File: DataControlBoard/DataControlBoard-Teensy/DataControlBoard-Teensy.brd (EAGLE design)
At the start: 66 x 88.9 mm, 40 parts, among them IC1 74LS165D, IC2 74LS165D, IC3 74AHC1G04DCK, J1 RS-Interface, J2 Pwr-Conn, J3 Static RPi, J4 Magnet RPi, J5 Boom Cam RPi, U1 MAX3232, U2 3V3REG

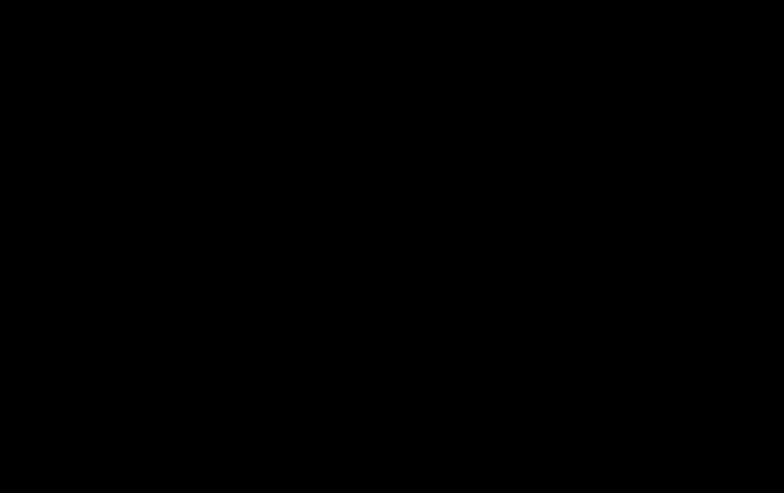
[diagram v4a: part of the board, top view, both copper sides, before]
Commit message: Minor schematic changes, added GND merges and header for LIDAR
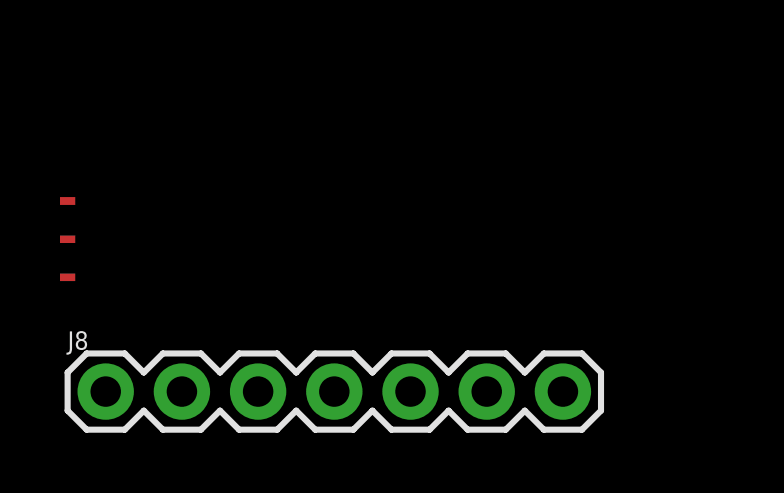
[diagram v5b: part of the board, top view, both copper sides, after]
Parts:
- added J8: (no value), SparkFun-Connectors:1X07
- added U$1, U$2, U$3: GND-MERGER, RPi-Parts:GND-MERGER
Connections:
- new net DTR: J8.2
- new net GND-ANALOG: J1.P21, U$1.P$2
- new net PDB-GND: J1.P7, U$3.P$2
- new net RX: J8.5
- new net TX: J8.6
- new net VS: J8.4
- new net VS_2: J8.1
- net GND: now also J8.3, J8.7, U$1.P$1, U$2.P$1, U$3.P$1; no longer J1.P18, J1.P19, J1.P21, J1.P7
- net PDB-STROBE-3V3: now also B1.22; no longer B1.2
- net RS232-GND: now also U$2.P$2
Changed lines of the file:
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@@
 <attribute name="VALUE" x="-71.12" y="-11.303" size="0.6096" layer="27" font="vector" ratio="20" align="top-center"/>
+</element>
+<element name="U$1" library="RPi-Parts" package="GND-MERGER" value="GND-MERGER" x="-85.09" y="-48.26" smashed="yes"/>
+<element name="U$2" library="RPi-Parts" package="GND-MERGER" value="GND-MERGER" x="-85.09" y="-49.53" smashed="yes"/>
+<element name="U$3" library="RPi-Parts" package="GND-MERGER" value="GND-MERGER" x="-85.09" y="-50.8" smashed="yes"/>
+<element name="J8" library="SparkFun-Connectors" library_urn="urn:adsk.eagle:library:513" package="1X07" package3d_urn="urn:adsk.eagle:package:38129/1" value="" x="-83.82" y="-54.61" smashed="yes">
+<attribute name="NAME" x="-85.09" y="-53.213" size="0.6096" layer="25" font="vector" ratio="20"/>
+<attribute name="VALUE" x="-85.09" y="-56.642" size="0.6096" layer="27" font="vector" ratio="20"/>
 </element>
 </elements>
 <signals>
 <signal name="GND">
-<contactref element="J1" pad="P24"/>
-<contactref element="J1" pad="P25"/>
-<contactref element="J1" pad="P7"/>
-<contactref element="J1" pad="P21"/>
-<contactref element="J1" pad="P19"/>
-<contactref element="J1" pad="P18"/>
 <contactref element="J1" pad="SHLD1"/>
 <contactref element="J1" pad="SHLD2"/>
@@
 <contactref element="C5" pad="2"/>
 <contactref element="IC3" pad="3"/>
+<contactref element="J1" pad="P25"/>
+<contactref element="J1" pad="P24"/>
+<contactref element="U$1" pad="P$1"/>
+<contactref element="U$2" pad="P$1"/>
+<contactref element="U$3" pad="P$1"/>
+<contactref element="J8" pad="7"/>
+<contactref element="J8" pad="3"/>
 <wire x1="87.63" y1="68.26" x2="92.71" y2="68.26" width="0" layer="19" extent="1-1"/>
 <wire x1="58.42" y1="85.09" x2="87.63" y2="68.26" width="0" layer="19" extent="1-1"/>
@@
 <wire x1="17.2466" y1="70.485" x2="23.3934" y2="78.105" width="0" layer="19" extent="1-1"/>
 <wire x1="17.145" y1="57.6834" x2="17.2466" y2="70.485" width="0" layer="19" extent="1-1"/>
-<wire x1="7.62" y1="55.88" x2="17.145" y2="57.6834" width="0" layer="19" extent="1-1"/>
-<wire x1="5.08" y1="55.245" x2="7.62" y2="55.88" width="0" layer="19" extent="1-1"/>
-<wire x1="5.08" y1="53.975" x2="5.08" y2="55.245" width="0" layer="19" extent="1-1"/>
-<wire x1="5.08" y1="57.785" x2="5.08" y2="55.245" width="0" layer="19" extent="1-1"/>
-<wire x1="5.08" y1="61.595" x2="5.08" y2="57.785" width="0" layer="19" extent="1-1"/>
+<wire x1="24.765" y1="51.5366" x2="17.145" y2="57.6834" width="0" layer="19" extent="1-1"/>
+<wire x1="5.08" y1="61.595" x2="17.145" y2="57.6834" width="0" layer="19" extent="1-1"/>
 <wire x1="5.08" y1="62.865" x2="5.08" y2="61.595" width="0" layer="19" extent="1-1"/>
 <wire x1="3.81" y1="68.1355" x2="5.08" y2="62.865" width="0" layer="19" extent="1-1"/>
-<wire x1="24.765" y1="51.5366" x2="17.145" y2="57.6834" width="0" layer="19" extent="1-1"/>
-<wire x1="3.81" y1="43.6245" x2="5.08" y2="53.975" width="0" layer="19" extent="1-1"/>
+<wire x1="3.81" y1="43.6245" x2="5.08" y2="61.595" width="0" layer="19" extent="1-1"/>
 <wire x1="3.81" y1="27.4955" x2="3.81" y2="43.6245" width="0" layer="19" extent="1-1"/>
 <wire x1="5.08" y1="15.875" x2="3.81" y2="27.4955" width="0" layer="19" extent="1-1"/>
@@
 <wire x1="-63.5" y1="47.31" x2="-63.5" y2="45.4" width="0" layer="19" extent="1-1"/>
 <wire x1="-73.01" y1="-4.66" x2="-63.5" y2="45.4" width="0" layer="19" extent="1-1"/>
+<wire x1="-85.217" y1="-48.26" x2="-73.01" y2="-4.66" width="0" layer="19" extent="1-1"/>
+<wire x1="-85.217" y1="-49.53" x2="-85.217" y2="-48.26" width="0" layer="19" extent="1-1"/>
+<wire x1="-85.217" y1="-50.8" x2="-85.217" y2="-49.53" width="0" layer="19" extent="1-1"/>
+<wire x1="-78.74" y1="-54.61" x2="-85.217" y2="-50.8" width="0" layer="19" extent="1-1"/>
+<wire x1="-68.58" y1="-54.61" x2="-78.74" y2="-54.61" width="0" layer="19" extent="1-1"/>
 </signal>
 <signal name="PDB13">
@@
 <signal name="RS232-GND">
 <contactref element="J1" pad="P23"/>
+<contactref element="U$2" pad="P$2"/>
+<wire x1="-84.963" y1="-49.53" x2="5.08" y2="60.325" width="0" layer="19" extent="1-1"/>
 </signal>
 <signal name="PDB12">
@@
 <contactref element="R7" pad="1"/>
 <contactref element="R8" pad="2"/>
-<contactref element="B1" pad="2"/>
+<contactref element="B1" pad="22"/>
+<wire x1="-18.1" y1="73.66" x2="46.99" y2="20.32" width="0" layer="19" extent="1-1"/>
 <wire x1="-20" y1="78.74" x2="-18.1" y2="73.66" width="0" layer="19" extent="1-1"/>
-<wire x1="62.23" y1="17.78" x2="-20" y2="78.74" width="0" layer="19" extent="1-1"/>
 </signal>
 <signal name="N$6">
@@
 <wire x1="-71.12" y1="-10.16" x2="33.655" y2="70.11" width="0" layer="19" extent="1-1"/>
 </signal>
+<signal name="PDB-GND">
+<contactref element="J1" pad="P7"/>
+<contactref element="U$3" pad="P$2"/>
+<wire x1="-84.963" y1="-50.8" x2="7.62" y2="55.88" width="0" layer="19" extent="1-1"/>
+</signal>
+<signal name="GND-ANALOG">
+<contactref element="J1" pad="P21"/>
+<contactref element="U$1" pad="P$2"/>
+<wire x1="-84.963" y1="-48.26" x2="5.08" y2="57.785" width="0" layer="19" extent="1-1"/>
+</signal>
+<signal name="TX">
+<contactref element="J8" pad="6"/>
+</signal>
+<signal name="RX">
+<contactref element="J8" pad="5"/>
+</signal>
+<signal name="VS">
+<contactref element="J8" pad="4"/>
+</signal>
+<signal name="DTR">
+<contactref element="J8" pad="2"/>
+</signal>
+<signal name="VS_2">
+<contactref element="J8" pad="1"/>
+</signal>
 </signals>

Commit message: Significant routing progress
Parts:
- removed J3: Static RPi, SparkFun-Connectors:2X5
- removed J4: Magnet RPi, SparkFun-Connectors:2X5
- removed J5: Boom Cam RPi, SparkFun-Connectors:2X5
- removed JP1: JUMPER-SMT_3_NO_NO-SILK, SparkFun-Jumpers:SMT-JUMPER_3_NO_NO-SILK
- added J10: Magnet RPi, SparkFun-Connectors:1X05_LOCK
- added J11: Boom Cam RPi, SparkFun-Connectors:1X05_LOCK
- added J9: Static RPi, SparkFun-Connectors:1X05_LOCK
- added PWR-SEL: JUMPER-SMT_3_NO_NO-SILK, SparkFun-Jumpers:SMT-JUMPER_3_NO_NO-SILK
- added TP10, TP11, TP12, TP13, TP14, TP15, TP16, TP17, TP18, TP19, TP20, TP8, TP9: TPPAD1-13, testpad:P1-13
- added TP4: GND, testpad:P1-13
- added TP5: 5V, testpad:P1-13
- added TP6: 3.3V, testpad:P1-13
- added TP7: STROBE, testpad:P1-13
- TP1, TP2, TP3: value TPPAD1-17 -> TPPAD1-13; device testpad:P1-17 -> testpad:P1-13
- moved IC3 143.3 mm to (58.4, 51.8), turned to 180 degrees
- moved U$3 142.2 mm to (8.89, 55.9), flipped to the bottom
- moved U$2 141.3 mm to (3.81, 60.3), flipped to the bottom, turned to 180 degrees
- moved UART-INV-SEL 140.8 mm to (56.8, 48.6), turned to 180 degrees
- moved U$1 138.4 mm to (3.81, 57.8), flipped to the bottom, turned to 180 degrees
- moved J8 130.9 mm to (34.0, 2.54), turned to 180 degrees
- moved C2 126.5 mm to (61.0, 21.6)
- moved C1 125.7 mm to (59.1, 76.2), turned to 90 degrees
- moved U2 119.2 mm to (61.3, 68.9), turned to 0 degrees
- moved R8 66.3 mm to (36.5, 37.5), turned to 180 degrees
- moved R7 65.9 mm to (32.4, 37.5), turned to 180 degrees
- moved C6 59.4 mm to (33.7, 74.0), turned to 180 degrees
- moved R4 47.6 mm to (32.1, 8.57), turned to 90 degrees
- moved R6 46.4 mm to (29.2, 8.57), turned to 90 degrees
- moved R3 45.4 mm to (38.4, 8.57), turned to 90 degrees
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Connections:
- removed net DTR: J8.2
- removed net LASER-UART-1: J2.P1
- removed net LASER-UART-2: J2.P2
- removed net LASER-UART-3: J2.P3
- removed net LASER-UART-4: J2.P4
- removed net LASER-UART-5: J2.P5
- removed net N$15: J4.6
- removed net N$16: J4.8
- removed net N$17: J4.10
- removed net N$18: J3.5
- removed net N$19: J3.7
- removed net N$21: J3.2
- removed net N$22: J3.4
- removed net N$23: J3.6
- removed net N$24: J3.8
- removed net N$25: J3.10
- removed net RX: J8.5
- removed net TX: J8.6
- removed net VS: J8.4
- removed net VS_2: J8.1
- new net +3.3V: TP6.TP
- new net LASER-DTR: J2.P4, J8.2
- new net LASER-RX: J2.P2, J8.5
- new net LASER-TX: J2.P1, J8.6
- new net LASER-VS-1: J2.P3, J8.4
- new net LASER-VS-2: J2.P5, J8.1
- new net N$1: B1.0, TP12.TP
- new net N$12: B1.21, TP11.TP
- net +5V: now also PWR-SEL.2, TP5.TP; no longer JP1.2
- net 5V-DIG-LASER: now also PWR-SEL.1; no longer JP1.1
- net 5V-DIG-MAG: now also PWR-SEL.3; no longer JP1.3
- net GND: now also TP4.TP
- net LAS-COMM-EN: now also J11.5; no longer J5.9
- net MAG-COMM-EN: now also J10.5; no longer J4.9
- net N$10: now also B1.15, TP9.TP; no longer J5.8
- net N$11: now also B1.20, TP10.TP; no longer J5.10
- net N$13: now also B1.6, TP19.TP; no longer J4.2
- net N$14: now also B1.7, TP20.TP; no longer J4.4
- net N$2: now also B1.1, TP13.TP; no longer J4.5
- net N$3: now also B1.2, TP14.TP; no longer J4.7
- net N$4: now also B1.9, TP15.TP; no longer J5.5
- net N$5: now also B1.13, TP16.TP; no longer J5.7
- net N$7: now also B1.12, TP17.TP; no longer J5.2
- net N$8: now also B1.11, TP18.TP; no longer J5.4
- net N$9: now also B1.14, TP8.TP; no longer J5.6
- net PDB-STROBE: now also TP7.TP
- net PI-SCL: now also J10.2, J11.2, J9.2; no longer J3.3, J4.3, J5.3
- net PI-SDA: now also J10.1, J11.1, J9.1; no longer J3.1, J4.1, J5.1
- net STA-COMM-EN: now also J9.5; no longer J3.9
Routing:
- net PDB16: track 0.00 -> 60.9 mm, vias 0 -> 2
- net PDB15: track 0.00 -> 55.2 mm, vias 0 -> 2
- net PDB14: track 0.00 -> 49.4 mm, vias 0 -> 2
- net PDB13: track 0.00 -> 41.8 mm, vias 0 -> 2
- net SDA0: track 0.00 -> 32.8 mm
- net LASER-VS-2: track 0.00 -> 30.6 mm
- net SDA1: track 0.00 -> 27.6 mm
- net LASER-DTR: track 0.00 -> 27.5 mm
- net PDB8: track 0.00 -> 26.4 mm, vias 0 -> 2
- net SHIFT-CLK: track 0.00 -> 25.3 mm, vias 0 -> 2
- net SHIFT-LAT: track 0.00 -> 24.5 mm, vias 0 -> 2
- net PDB7: track 0.00 -> 24.1 mm, vias 0 -> 2
- net LASER-VS-1: track 0.00 -> 21.9 mm
- net SCL0: track 0.00 -> 21.6 mm
- net PDB9: track 0.00 -> 21.5 mm
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- added copper zone on layer 1, net +3V3
- added copper zone on layer 16, net GND
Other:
- board text added: "Enable Layers 108/200 for RPi Footprint"
- board text added: "RPi"
- board text added: "ToDo: Add labels for I2C Selections grid"
- board text removed: "Note: Connector sizes might be off. Stay 100 mil away from connector housing front to back"

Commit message: Fully routed. Needs minor changes
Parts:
- moved TP6 86.8 mm to (2.48, 38.0)
- moved TP4 77.5 mm to (2.48, 34.2)
- moved TP7 74.1 mm to (6.29, 38.0)
- moved TP5 74.1 mm to (28.3, 47.9)
- moved C1 61.8 mm to (19.2, 29.0), turned to 270 degrees
- moved U2 47.5 mm to (19.8, 45.7), turned to 90 degrees
- moved IC3 46.7 mm to (43.2, 7.56)
- moved UART-INV-SEL 41.9 mm to (48.5, 7.56), turned to 90 degrees
- moved PWR-SEL 37.3 mm to (26.2, 47.9), turned to 270 degrees
- moved R2 20.3 mm to (46.0, 34.4)
- moved J10 20.3 mm to (48.3, 43.3)
- moved J11 20.3 mm to (48.3, 47.1)
- moved J9 20.3 mm to (48.3, 39.5)
- moved R1 20.3 mm to (48.3, 34.4)
- moved R8 5.91 mm to (31.2, 34.9)
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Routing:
- net 5V-DIG-LASER: track 0.00 -> 118.6 mm, vias 0 -> 3
- net 5V-DIG-MAG: track 0.00 -> 107.1 mm
- net 5V-DIG-STA: track 0.00 -> 104.3 mm, vias 0 -> 1
- net 5V-DIG-CAM: track 0.00 -> 103.4 mm
- net 5V-DIG-TX: track 0.00 -> 102.6 mm
- net N$20: track 0.00 -> 90.6 mm, vias 0 -> 2
- net SHIFT-IN: track 21.3 -> 87.5 mm, vias 0 -> 3
- net SHIFT-LAT: track 24.5 -> 80.2 mm, vias 2 -> 4
- net RS232-DATA: track 0.00 -> 52.5 mm, vias 0 -> 2
- net SHIFT-CLK: track 25.3 -> 76.6 mm, vias 2 -> 4
- net PI-SDA: track 11.6 -> 56.2 mm
- net PI-SCL: track 12.0 -> 55.4 mm, vias 0 -> 1
- net PDB-STROBE: track 12.3 -> 54.8 mm, vias 0 -> 2
- net SCL1: track 15.7 -> 56.5 mm, vias 0 -> 3
- net SCL0: track 21.6 -> 53.7 mm, vias 0 -> 1
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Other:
- board text added: "ToDo: Label Power Test Points"
- board text added: "ToDo: Mounting holes for RPi"

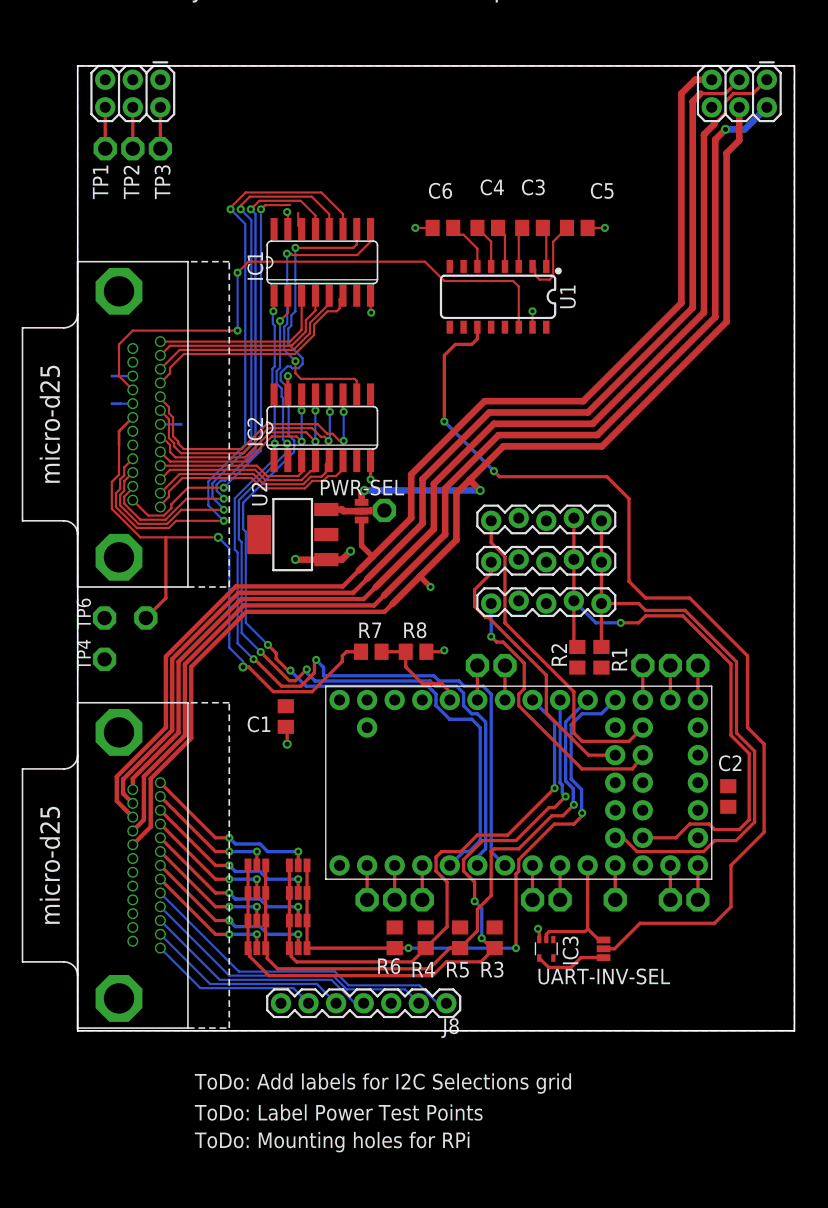
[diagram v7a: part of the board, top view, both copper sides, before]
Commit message: Added mounting holes and rounded corners
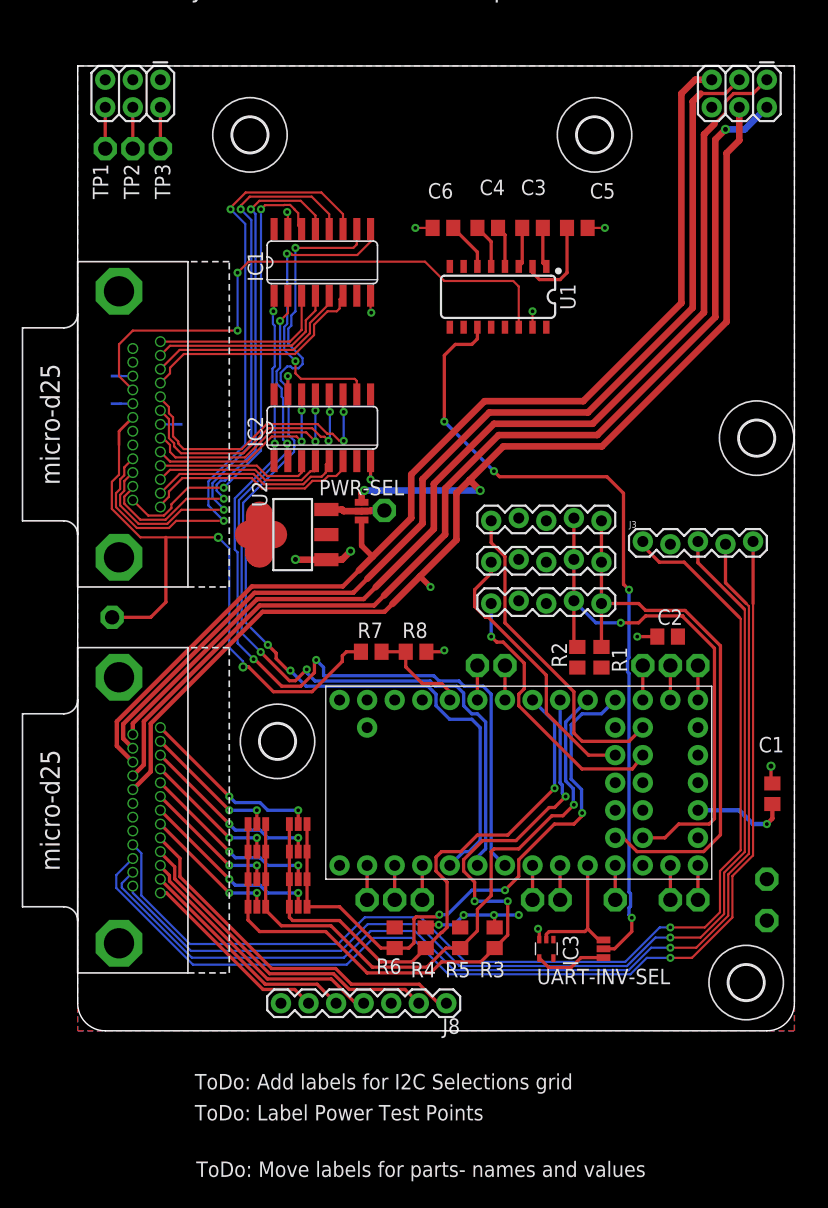
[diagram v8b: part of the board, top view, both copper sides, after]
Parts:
- added H1, H2, H3, H4, H5: MOUNT-HOLE3.2, holes:3,2
- added J3: Antenna SPI, SparkFun-Connectors:1X05_LOCK
- moved TP6 67.1 mm to (63.5, 10.2)
- moved TP4 64.3 mm to (63.5, 14.0)
- moved C1 45.4 mm to (64.0, 21.8), turned to 90 degrees
- moved C2 15.8 mm to (54.4, 36.3), turned to 180 degrees
- moved J2 5.08 mm to (7.62, 20.3)
- moved SCL-SEL2 3.81 mm to (20.3, 16.5)
- moved SDA-SEL2 3.81 mm to (16.5, 16.5)
- moved SCL-SEL1 3.81 mm to (20.3, 14.0)
- moved SCL-SEL3 3.81 mm to (20.3, 19.1)
- moved SDA-SEL1 3.81 mm to (16.5, 14.0)
- moved SDA-SEL3 3.81 mm to (16.5, 19.1)
- moved SCL-SEL0 3.81 mm to (20.3, 11.4)
- moved SDA-SEL0 3.81 mm to (16.5, 11.4)
- moved TP7 3.11 mm to (3.17, 38.1)
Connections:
- removed net N$30: J2.P18
- removed net N$31: J2.P19
- net ANT-MISO: now also J3.4
- net ANT-MOSI: now also J3.3
- net ANT-SCK: now also J3.5
- net ANT-SS: now also J3.1
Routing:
- net ANT-SS: track 0.00 -> 104.8 mm, vias 0 -> 1
- net ANT-SCK: track 0.00 -> 103.0 mm, vias 0 -> 1
- net ANT-MISO: track 0.00 -> 100.9 mm, vias 0 -> 1
- net ANT-MOSI: track 0.00 -> 98.8 mm, vias 0 -> 1
- net +3V3: track 0.00 -> 25.3 mm, vias 0 -> 5
- net N$20: track 90.6 -> 74.3 mm, vias 2 -> 4
- net 5V-DIG-LASER: track 118.6 -> 112.5 mm
- net 5V-DIG-TX: track 102.6 -> 96.7 mm
- net 5V-DIG-STA: track 104.3 -> 98.3 mm
- net 5V-DIG-MAG: track 107.1 -> 101.1 mm
- net 5V-DIG-CAM: track 103.4 -> 97.5 mm
- net PI-SCL: track 55.4 -> 50.4 mm
- net SDA0: track 63.2 -> 67.6 mm
- net PI-SDA: track 56.2 -> 52.5 mm
- net PDB-STROBE: track 54.8 -> 58.1 mm
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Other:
- outline, holes or cut-outs redrawn
- board text added: "ToDo: Move labels for parts- names and values"
- board text removed: "ToDo: Mounting holes for RPi"
